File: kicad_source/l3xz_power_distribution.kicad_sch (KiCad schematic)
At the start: 28 parts, among them J1 PowerPole_ver, J10 PowerPole_ver, J11 PowerPole_ver, J12 PowerPole_ver, J2 PowerPole_ver, J3 PowerPole_ver, J4 PowerPole_ver, J5 PowerPole_ver, J6 PowerPole_ver, J7 PowerPole_ver, J8 PowerPole_ver, J9 PowerPole_ver

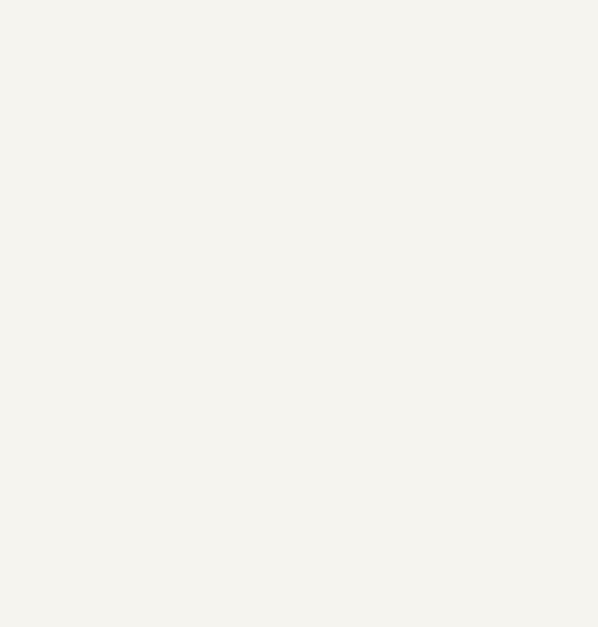
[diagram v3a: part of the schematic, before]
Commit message: added mounting holes
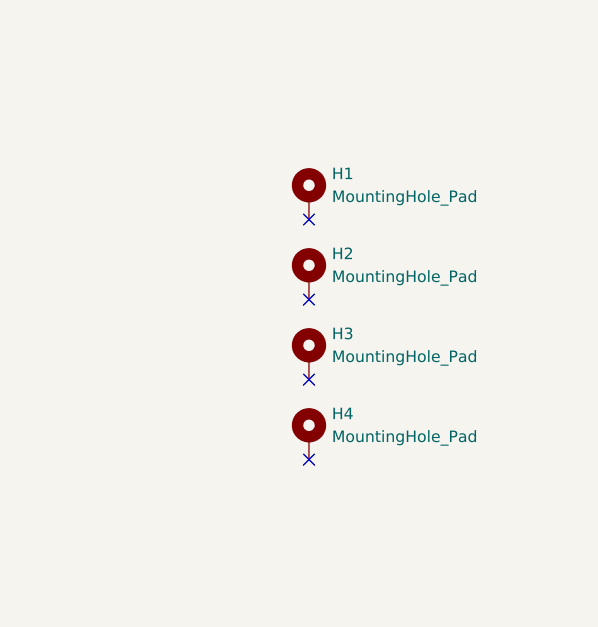
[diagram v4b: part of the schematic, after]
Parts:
- added H1: MountingHole_Pad, symbol Mechanical:MountingHole_Pad
- added H2, H3, H4: MountingHole_Pad, MountingHole:MountingHole_3.2mm_M3_DIN965_Pad, symbol Mechanical:MountingHole_Pad
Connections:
- no-connect marks 0 -> 4
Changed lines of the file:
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@@
     (company "107-systems")
   )
+  (no_connect (at 248.92 113.03))
+  (no_connect (at 248.92 95.25))
+  (no_connect (at 248.92 104.14))
+  (no_connect (at 248.92 121.92))
   (wire (pts (xy 182.88 143.51) (xy 182.88 146.05))
     (stroke (width 0) (type default) (color 0 0 0 0))
@@
     (pin "1")
   )
+  (symbol (lib_id "Mechanical:MountingHole_Pad") (at 248.92 101.6 0) (unit 1)
+    (in_bom yes) (on_board yes) (fields_autoplaced)
+    (property "Reference" "H2" (id 0) (at 251.46 99.0599 0)
+      (effects (font (size 1.27 1.27)) (justify left))
+    )
+    (property "Value" "MountingHole_Pad" (id 1) (at 251.46 101.5999 0)
+      (effects (font (size 1.27 1.27)) (justify left))
+    )
+    (property "Footprint" "MountingHole:MountingHole_3.2mm_M3_DIN965_Pad" (id 2) (at 248.92 101.6 0)
+      (effects (font (size 1.27 1.27)) hide)
+    )
+    (property "Datasheet" "~" (id 3) (at 248.92 101.6 0)
+      (effects (font (size 1.27 1.27)) hide)
+    )
+    (pin "1")
+  )
   (symbol (lib_id "power:GND") (at 142.24 182.88 0) (unit 1)
     (in_bom yes) (on_board yes) (fields_autoplaced)
@@
     (pin "2")
   )
+  (symbol (lib_id "Mechanical:MountingHole_Pad") (at 248.92 110.49 0) (unit 1)
+    (in_bom yes) (on_board yes) (fields_autoplaced)
+    (property "Reference" "H3" (id 0) (at 251.46 107.9499 0)
+      (effects (font (size 1.27 1.27)) (justify left))
+    )
+    (property "Value" "MountingHole_Pad" (id 1) (at 251.46 110.4899 0)
+      (effects (font (size 1.27 1.27)) (justify left))
+    )
+    (property "Footprint" "MountingHole:MountingHole_3.2mm_M3_DIN965_Pad" (id 2) (at 248.92 110.49 0)
+      (effects (font (size 1.27 1.27)) hide)
+    )
+    (property "Datasheet" "~" (id 3) (at 248.92 110.49 0)
+      (effects (font (size 1.27 1.27)) hide)
+    )
+    (pin "1")
+  )
   (symbol (lib_id "Connector_Generic:Conn_01x02") (at 73.66 113.03 0) (unit 1)
     (in_bom yes) (on_board yes) (fields_autoplaced)
@@
     (pin "1")
   )
+  (symbol (lib_id "Mechanical:MountingHole_Pad") (at 248.92 92.71 0) (unit 1)
+    (in_bom yes) (on_board yes) (fields_autoplaced)
+    (property "Reference" "H1" (id 0) (at 251.46 90.1699 0)
+      (effects (font (size 1.27 1.27)) (justify left))
+    )
+    (property "Value" "MountingHole_Pad" (id 1) (at 251.46 92.7099 0)
+      (effects (font (size 1.27 1.27)) (justify left))
+    )
+    (property "Footprint" "" (id 2) (at 248.92 92.71 0)
+      (effects (font (size 1.27 1.27)) hide)
+    )
+    (property "Datasheet" "~" (id 3) (at 248.92 92.71 0)
+      (effects (font (size 1.27 1.27)) hide)
+    )
+    (pin "1")
+  )
   (symbol (lib_id "Device:C_Small") (at 49.53 135.89 0) (unit 1)
     (in_bom yes) (on_board yes) (fields_autoplaced)
@@
     (pin "1")
     (pin "2")
+  )
+  (symbol (lib_id "Mechanical:MountingHole_Pad") (at 248.92 119.38 0) (unit 1)
+    (in_bom yes) (on_board yes) (fields_autoplaced)
+    (property "Reference" "H4" (id 0) (at 251.46 116.8399 0)
+      (effects (font (size 1.27 1.27)) (justify left))
+    )
+    (property "Value" "MountingHole_Pad" (id 1) (at 251.46 119.3799 0)
+      (effects (font (size 1.27 1.27)) (justify left))
+    )
+    (property "Footprint" "MountingHole:MountingHole_3.2mm_M3_DIN965_Pad" (id 2) (at 248.92 119.38 0)
+      (effects (font (size 1.27 1.27)) hide)
+    )
+    (property "Datasheet" "~" (id 3) (at 248.92 119.38 0)
+      (effects (font (size 1.27 1.27)) hide)
+    )
+    (pin "1")
   )
   (symbol (lib_id "power:GND") (at 142.24 118.11 0) (unit 1)
@@
       (reference "D1") (unit 1) (value "LED_Small") (footprint "LED_SMD:LED_0603_1608Metric")
     )
+    (path "/6a7e0bf4-f960-4745-8dd2-66806c9968e5"
+      (reference "H1") (unit 1) (value "MountingHole_Pad") (footprint "MountingHole:MountingHole_3.2mm_M3_DIN965_Pad")
+    )
+    (path "/2a57b595-35f3-43b6-991d-2c55bee83dbd"
+      (reference "H2") (unit 1) (value "MountingHole_Pad") (footprint "MountingHole:MountingHole_3.2mm_M3_DIN965_Pad")
+    )
+    (path "/4bf36584-71dc-48b1-8b05-8ab78f6a8068"
+      (reference "H3") (unit 1) (value "MountingHole_Pad") (footprint "MountingHole:MountingHole_3.2mm_M3_DIN965_Pad")
+    )
+    (path "/c2971403-9ea3-4d2d-b4dc-8b2d3538422b"
+      (reference "H4") (unit 1) (value "MountingHole_Pad") (footprint "MountingHole:MountingHole_3.2mm_M3_DIN965_Pad")
+    )
     (path "/40ba9434-20aa-4351-8c1b-12ceb107b778"

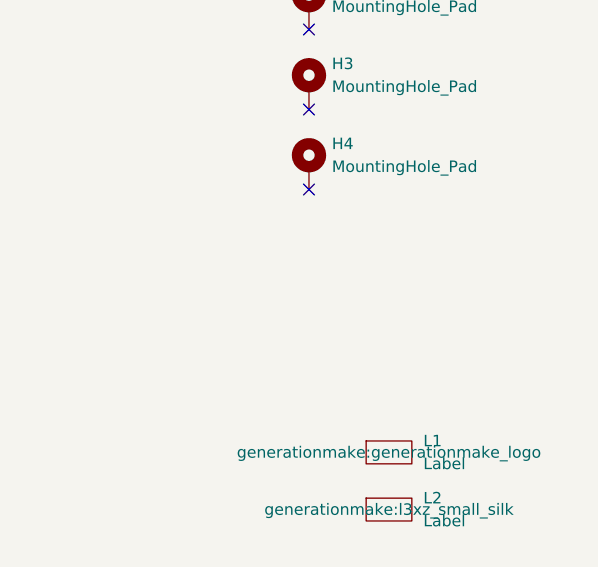
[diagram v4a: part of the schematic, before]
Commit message: added additional mounting hole
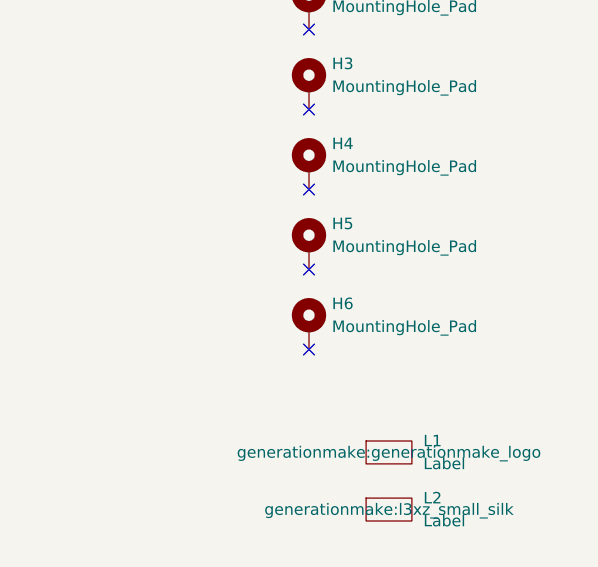
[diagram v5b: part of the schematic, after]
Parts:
- added H5, H6: MountingHole_Pad, MountingHole:MountingHole_3.2mm_M3_DIN965_Pad, symbol Mechanical:MountingHole_Pad
- H1: footprint (none) -> MountingHole:MountingHole_3.2mm_M3_DIN965_Pad
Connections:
- no-connect marks 4 -> 6
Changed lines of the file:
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@@
   (title_block
     (title "l3xz_power_distribution")
-    (date "2023-04-08")
+    (date "2023-04-09")
     (rev "0.1")
     (company "107-systems")
   )
+  (no_connect (at 248.92 139.7))
   (no_connect (at 248.92 113.03))
+  (no_connect (at 248.92 130.81))
   (no_connect (at 248.92 95.25))
   (no_connect (at 248.92 104.14))
@@
       (effects (font (size 1.27 1.27)) (justify left))
     )
-    (property "Footprint" "" (id 2) (at 248.92 92.71 0)
+    (property "Footprint" "MountingHole:MountingHole_3.2mm_M3_DIN965_Pad" (id 2) (at 248.92 92.71 0)
       (effects (font (size 1.27 1.27)) hide)
     )
@@
     (pin "1")
     (pin "2")
+  )
+  (symbol (lib_id "Mechanical:MountingHole_Pad") (at 248.92 128.27 0) (unit 1)
+    (in_bom yes) (on_board yes) (fields_autoplaced)
+    (property "Reference" "H5" (id 0) (at 251.46 125.7299 0)
+      (effects (font (size 1.27 1.27)) (justify left))
+    )
+    (property "Value" "MountingHole_Pad" (id 1) (at 251.46 128.2699 0)
+      (effects (font (size 1.27 1.27)) (justify left))
+    )
+    (property "Footprint" "MountingHole:MountingHole_3.2mm_M3_DIN965_Pad" (id 2) (at 248.92 128.27 0)
+      (effects (font (size 1.27 1.27)) hide)
+    )
+    (property "Datasheet" "~" (id 3) (at 248.92 128.27 0)
+      (effects (font (size 1.27 1.27)) hide)
+    )
+    (pin "1")
   )
   (symbol (lib_id "power:+BATT") (at 66.04 24.13 0) (unit 1)
@@
     )
     (property "Datasheet" "" (id 3) (at 66.04 45.72 0)
+      (effects (font (size 1.27 1.27)) hide)
+    )
+    (pin "1")
+  )
+  (symbol (lib_id "Mechanical:MountingHole_Pad") (at 248.92 137.16 0) (unit 1)
+    (in_bom yes) (on_board yes) (fields_autoplaced)
+    (property "Reference" "H6" (id 0) (at 251.46 134.6199 0)
+      (effects (font (size 1.27 1.27)) (justify left))
+    )
+    (property "Value" "MountingHole_Pad" (id 1) (at 251.46 137.1599 0)
+      (effects (font (size 1.27 1.27)) (justify left))
+    )
+    (property "Footprint" "MountingHole:MountingHole_3.2mm_M3_DIN965_Pad" (id 2) (at 248.92 137.16 0)
+      (effects (font (size 1.27 1.27)) hide)
+    )
+    (property "Datasheet" "~" (id 3) (at 248.92 137.16 0)
       (effects (font (size 1.27 1.27)) hide)
     )
@@
       (reference "H4") (unit 1) (value "MountingHole_Pad") (footprint "MountingHole:MountingHole_3.2mm_M3_DIN965_Pad")
     )
+    (path "/7041093c-e64c-451f-8ae6-b9c314fadbd7"
+      (reference "H5") (unit 1) (value "MountingHole_Pad") (footprint "MountingHole:MountingHole_3.2mm_M3_DIN965_Pad")
+    )
+    (path "/cdeee3d0-bf98-4cd1-9d4d-9df40e15b216"
+      (reference "H6") (unit 1) (value "MountingHole_Pad") (footprint "MountingHole:MountingHole_3.2mm_M3_DIN965_Pad")
+    )
     (path "/40ba9434-20aa-4351-8c1b-12ceb107b778"

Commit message: switched to THT for LED and resistor
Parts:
- D1: footprint LED_SMD:LED_0603_1608Metric -> LED_THT:LED_D3.0mm
- R1: footprint Resistor_SMD:R_0603_1608Metric -> Resistor_THT:R_Axial_DIN0207_L6.3mm_D2.5mm_P7.62mm_Horizontal
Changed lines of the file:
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@@
       (effects (font (size 1.27 1.27)) (justify left))
     )
-    (property "Footprint" "Resistor_SMD:R_0603_1608Metric" (id 2) (at 182.88 132.08 0)
+    (property "Footprint" "Resistor_THT:R_Axial_DIN0207_L6.3mm_D2.5mm_P7.62mm_Horizontal" (id 2) (at 182.88 132.08 0)
       (effects (font (size 1.27 1.27)) hide)
     )
@@
       (effects (font (size 1.27 1.27)) (justify right))
     )
-    (property "Footprint" "LED_SMD:LED_0603_1608Metric" (id 2) (at 182.88 140.97 90)
+    (property "Footprint" "LED_THT:LED_D3.0mm" (id 2) (at 182.88 140.97 90)
       (effects (font (size 1.27 1.27)) hide)
     )
@@
     )
     (path "/aa33507a-d84b-4086-beae-008cffa3c4b6"
-      (reference "D1") (unit 1) (value "LED_Small") (footprint "LED_SMD:LED_0603_1608Metric")
+      (reference "D1") (unit 1) (value "LED_Small") (footprint "LED_THT:LED_D3.0mm")
     )
     (path "/6a7e0bf4-f960-4745-8dd2-66806c9968e5"
@@
     )
     (path "/5a85479c-fca6-4da9-9ced-dadc3e18f6c4"
-      (reference "R1") (unit 1) (value "10k") (footprint "Resistor_SMD:R_0603_1608Metric")
-    )
-  )
+      (reference "R1") (unit 1) (value "10k") (footprint "Resistor_THT:R_Axial_DIN0207_L6.3mm_D2.5mm_P7.62mm_Horizontal")
+    )
+  )

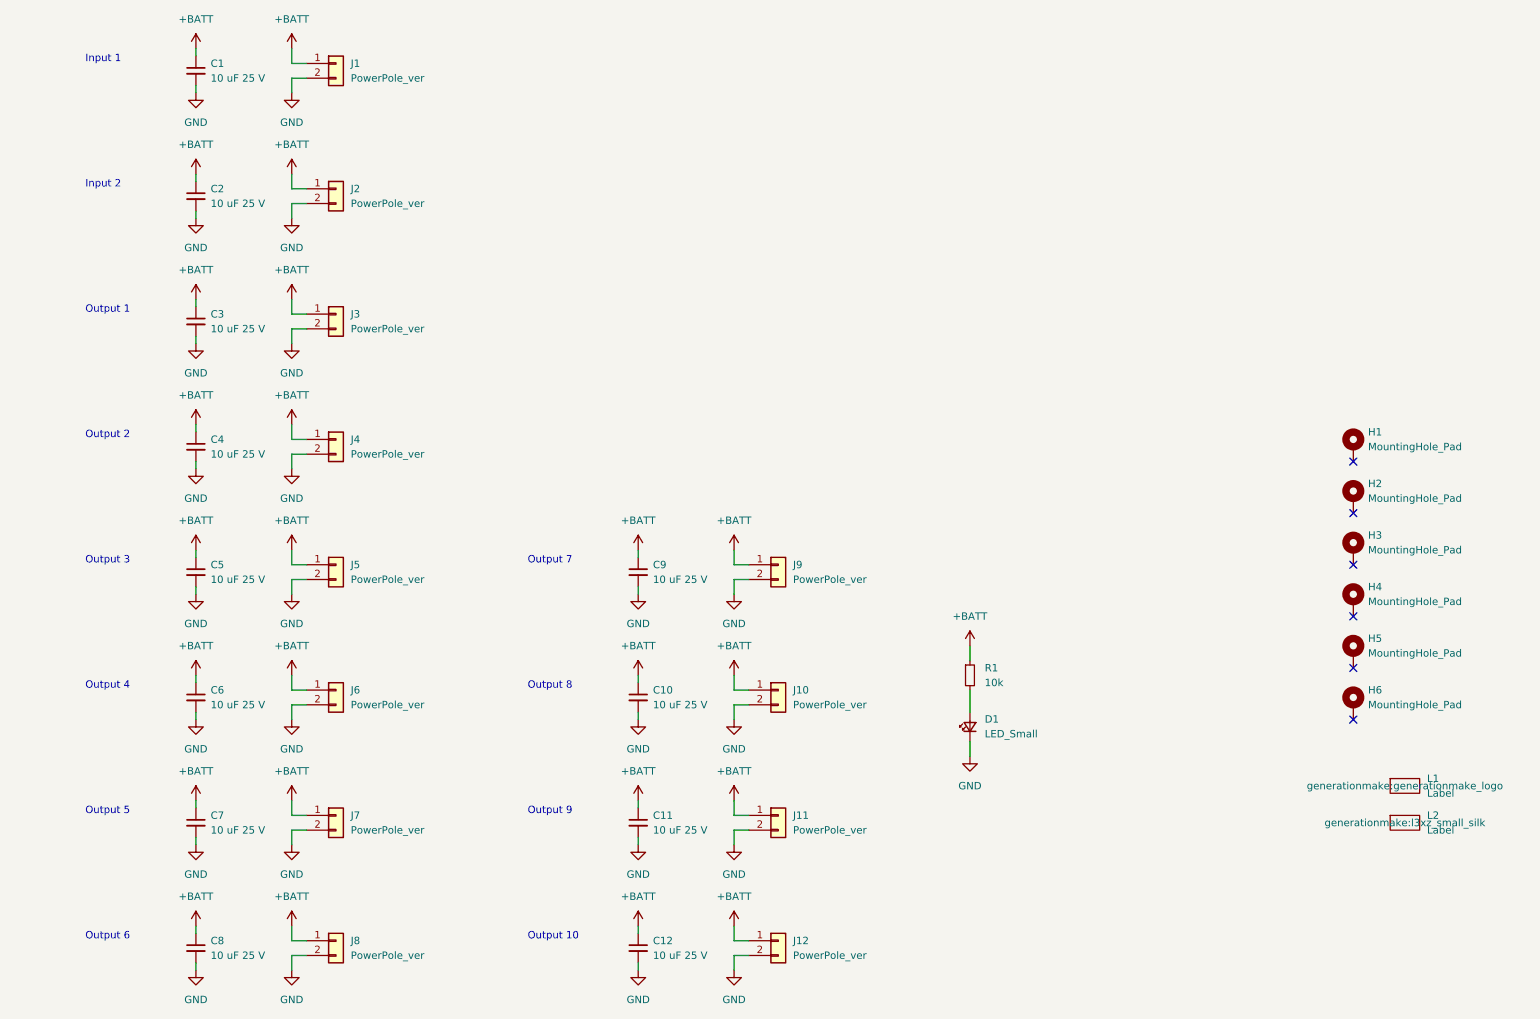
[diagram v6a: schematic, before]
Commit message: added alternative footprint for power pole
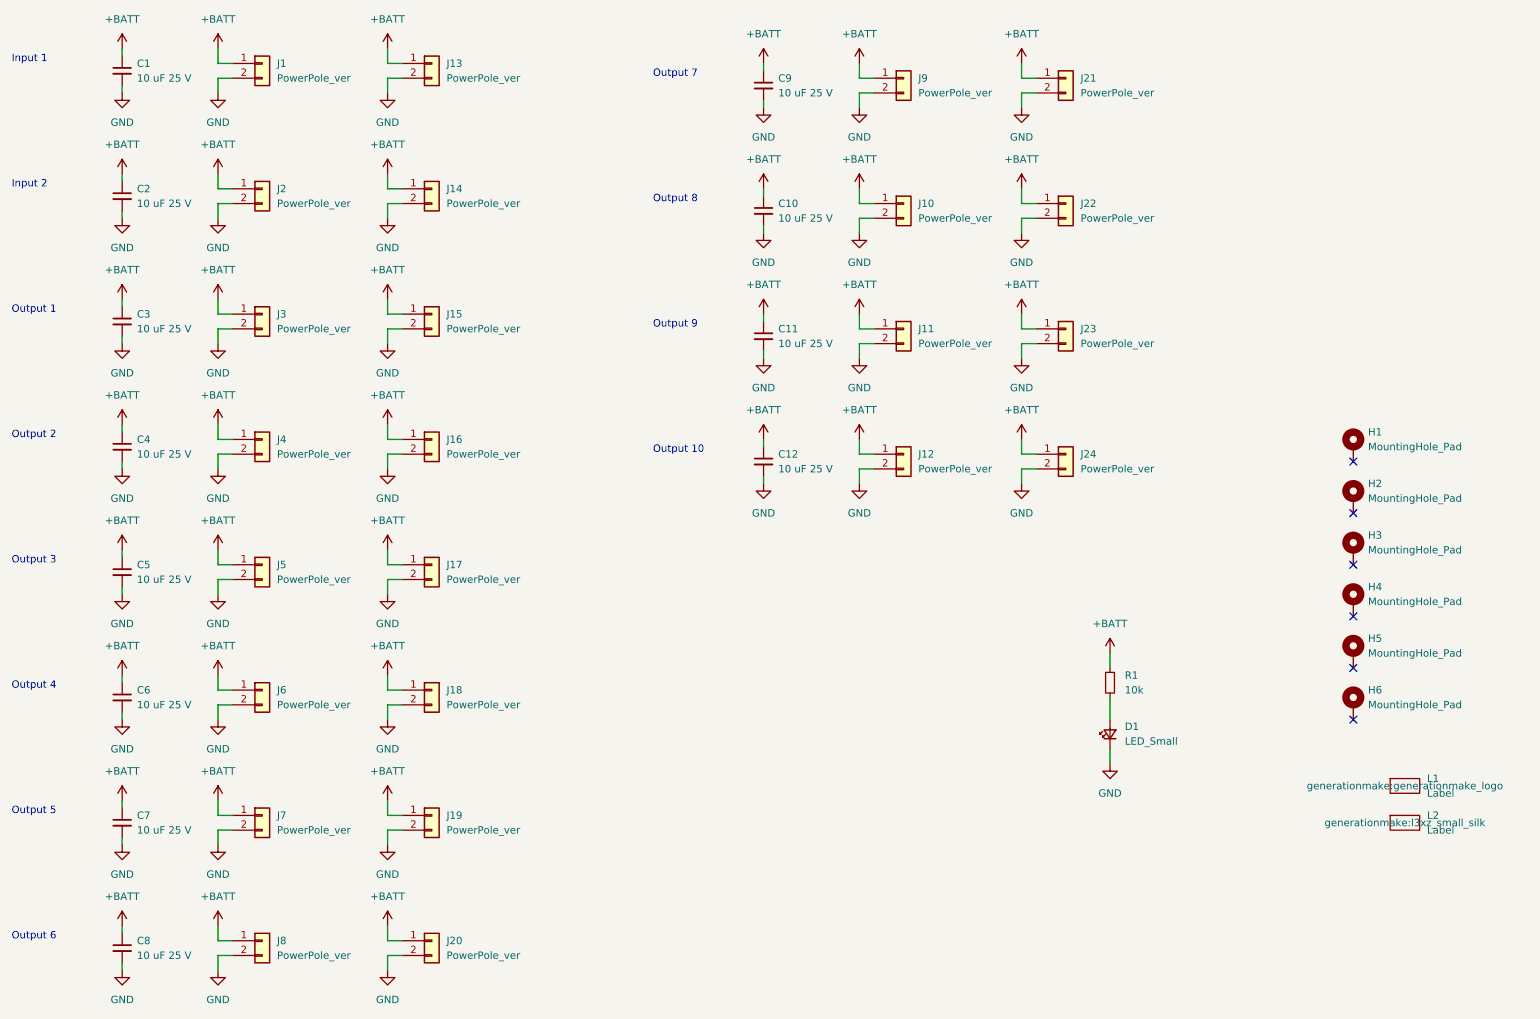
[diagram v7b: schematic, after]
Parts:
- added J13, J14, J15, J16, J17, J18, J19, J20, J21, J22, J23, J24: PowerPole_ver, generationmake:POWERPOLE_2, symbol Connector_Generic:Conn_01x02
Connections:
- net +BATT: now also J13.1 (Pin_1), J14.1 (Pin_1), J15.1 (Pin_1), J16.1 (Pin_1), J17.1 (Pin_1), J18.1 (Pin_1), J19.1 (Pin_1), J20.1 (Pin_1), J21.1 (Pin_1), J22.1 (Pin_1), J23.1 (Pin_1), J24.1 (Pin_1)
- net GND: now also J13.2 (Pin_2), J14.2 (Pin_2), J15.2 (Pin_2), J16.2 (Pin_2), J17.2 (Pin_2), J18.2 (Pin_2), J19.2 (Pin_2), J20.2 (Pin_2), J21.2 (Pin_2), J22.2 (Pin_2), J23.2 (Pin_2), J24.2 (Pin_2)
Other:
- moved on the sheet: C1, C10, C11, C12, C2, C3, C4, C5, C6, C7, C8, C9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
